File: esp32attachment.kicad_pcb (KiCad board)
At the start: 2 copper layers, 157.1 x 57.6 mm, 42 parts, among them J1 Conn_01x02, J2 Conn_01x02, J3 Conn_01x02, J4 Conn_01x02, J5 Conn_01x02, J6 Conn_01x02, J8 Conn_01x02, Q1 AOD4184A, Q2 AOD4184A, Q3 AOD4184A, Q4 AOD4184A, Q5 AOD4184A, Q6 AOD4184A, U1 ESP32-DEVKIT-V1, U2 PC847, U3 PC827

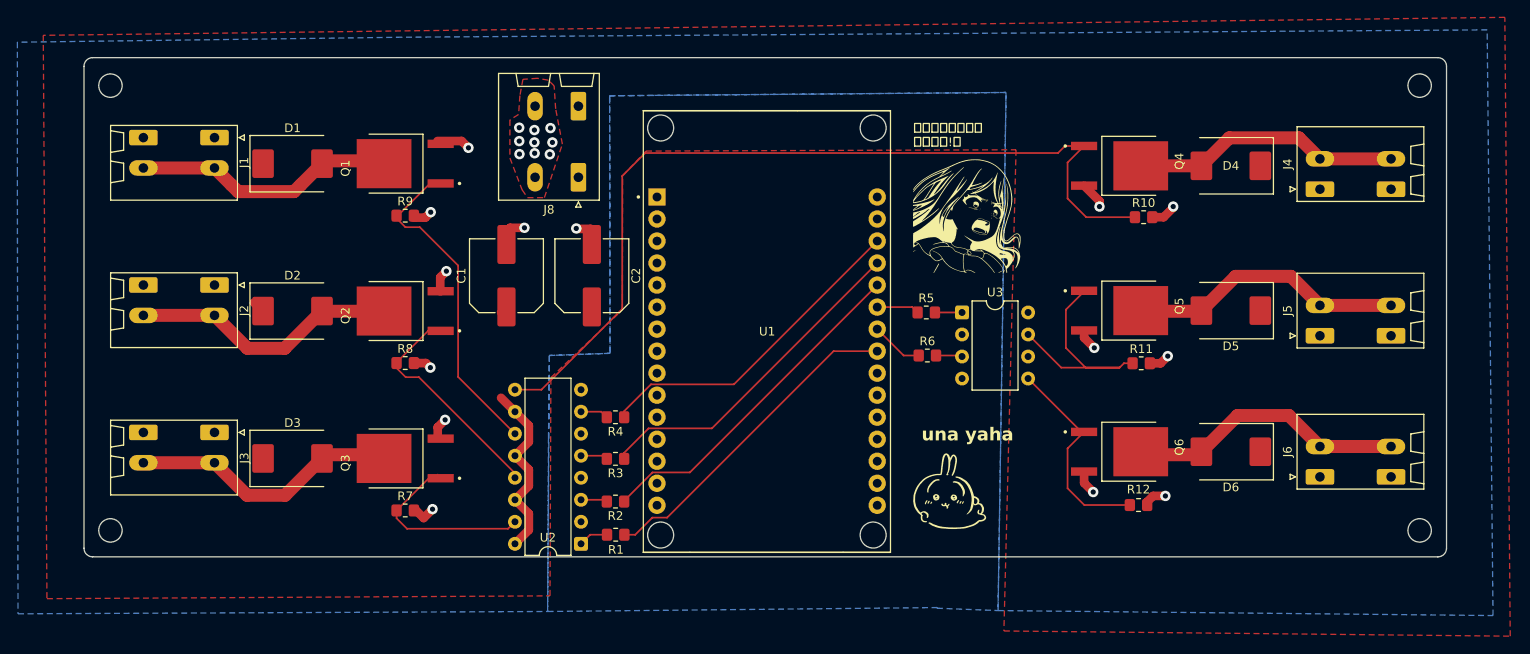
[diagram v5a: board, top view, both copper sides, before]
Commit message: added screw terminals and sakikoooo
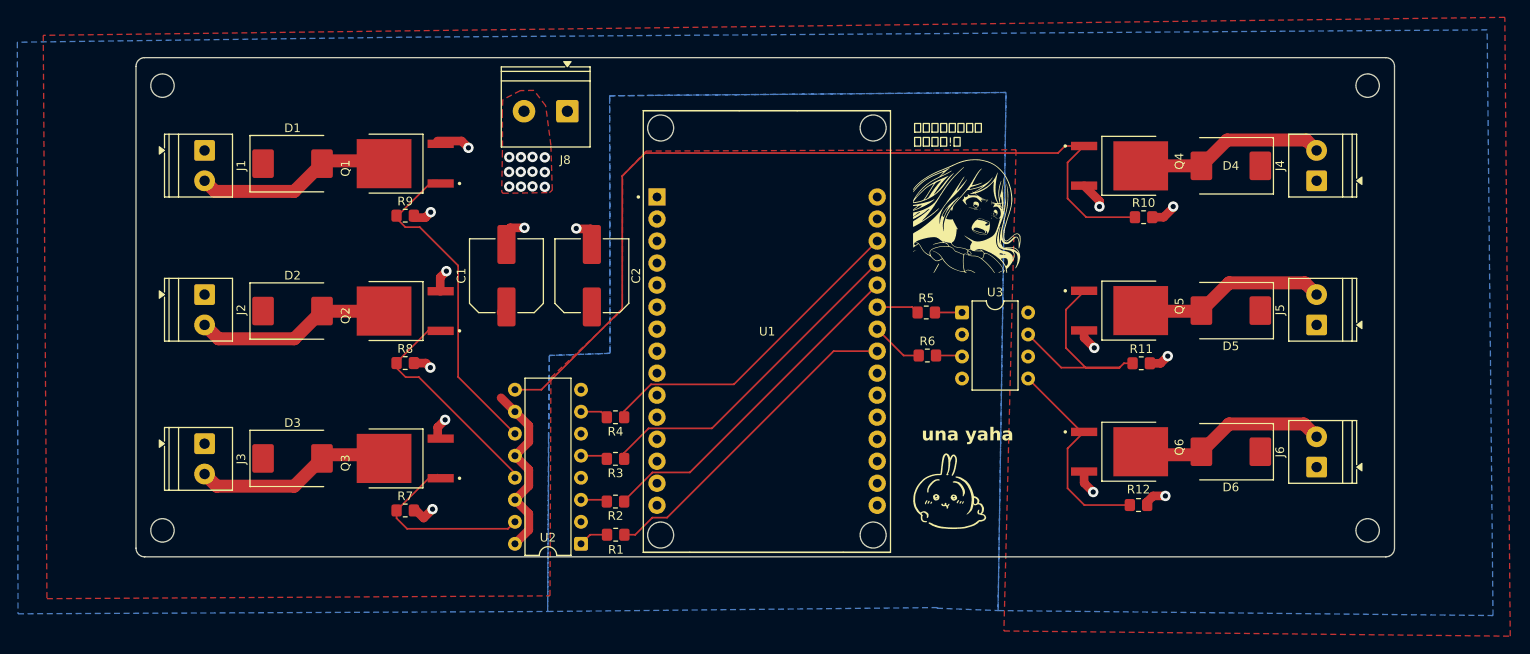
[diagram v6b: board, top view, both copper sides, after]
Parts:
- added G***: LOGO, symbols:sakistand, B.Cu at (71.5, 65.2)
- J1, J2, J3, J4, J5, J6: footprint Connector_Phoenix_SPT:PhoenixContact_SPT_1.5_2-H-3.5_1x02_P3.5mm_Horizontal -> TerminalBlock_Phoenix:TerminalBlock_Phoenix_PT-1,5-2-3.5-H_1x02_P3.50mm_Horizontal
- J8: footprint Connector_Phoenix_SPT:PhoenixContact_SPT_2.5_2-H-5.0_1x02_P5.0mm_Horizontal -> TerminalBlock_Phoenix:TerminalBlock_Phoenix_PT-1,5-2-5.0-H_1x02_P5.00mm_Horizontal
- moved J8 7.72 mm to (101.7, 48.0)
- moved REF** 6.00 mm to (194.0, 45.0)
- moved REF** 6.00 mm to (55.0, 96.3)
- moved REF** 6.00 mm to (194.0, 96.3)
- moved REF** 6.00 mm to (55.0, 45.0)
- moved J1 1.87 mm to (59.9, 52.5)
- moved J3 1.73 mm to (59.9, 86.3)
- moved J2 1.59 mm to (59.9, 69.1)
- moved J5 1.31 mm to (188.1, 72.6)
- moved J6 1.19 mm to (188.1, 89.0)
- moved J4 1.05 mm to (188.1, 56.0)
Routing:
- net /FET_DRAIN6: track 32.1 -> 22.2 mm
- net /FET_DRAIN5: track 31.9 -> 22.2 mm
- net /FET_DRAIN4: track 31.2 -> 22.0 mm
- net /FET_DRAIN3: track 30.8 -> 22.3 mm
- net /FET_DRAIN2: track 31.1 -> 22.7 mm
- net /FET_DRAIN1: track 29.9 -> 22.3 mm
- net +12V: track 24.7 -> 22.4 mm
- net GNDPWR: vias 23 -> 26
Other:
- board size 157.1 x 57.6 mm -> 145.1 x 57.6 mm

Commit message: minor changes and silkscreen update
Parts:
- removed the G*** at (71.5, 65.2)
- added G***: LOGO, symbols:kangelf, B.Cu at (125.3, 73.4)
- added G***: LOGO, symbols:sakidarker, B.Cu at (75.9, 60.1)
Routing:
- net +12V: track 22.4 -> 0.88 mm
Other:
- board text added: "インターネット や・め・ろ～！！！"
